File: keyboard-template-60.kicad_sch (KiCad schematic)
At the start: 168 parts, among them J1 USB_C_Receptacle_USB2.0, J2 Conn_01x04_MountingPin, SW1 SW_Reset, U1 ATmega32U4-M, U2 SRV05-4, Y1 16MHz

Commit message: Gerbers
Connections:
- net GND: now also U1.45 (Secure_to_PCB)
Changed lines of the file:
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@@
+    (stroke (width 0) (type default) (color 0 0 0 0))
+  )
+  (wire (pts (xy 346.71 127) (xy 353.06 127))
     (stroke (width 0) (type default) (color 0 0 0 0))
   )
@@
     (pin "43")
     (pin "44")
+    (pin "45")
     (pin "5")
     (pin "6")

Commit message: Update schematics and BOM
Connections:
- net COL1: now also U1.11 (PB3); no longer U1.38 (PF5)
- net ROW4: now also U1.38 (PF5); no longer U1.39 (PF4)
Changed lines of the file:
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@@
     )
   )
-  (global_label "ROW4" (shape input) (at 370.84 109.22 0) (fields_autoplaced)
+  (global_label "ROW4" (shape input) (at 370.84 111.76 0) (fields_autoplaced)
     (effects (font (size 1.27 1.27)) (justify left))
-    (property "Intersheet References" "${INTERSHEET_REFS}" (id 0) (at 378.5145 109.2994 0)
+    (property "Intersheet References" "${INTERSHEET_REFS}" (id 0) (at 378.5145 111.8394 0)
       (effects (font (size 1.27 1.27)) (justify left) hide)
     )
@@
     )
   )
-  (global_label "COL1" (shape input) (at 370.84 111.76 0) (fields_autoplaced)
+  (global_label "COL1" (shape input) (at 370.84 50.8 0) (fields_autoplaced)
     (effects (font (size 1.27 1.27)) (justify left))
-    (property "Intersheet References" "${INTERSHEET_REFS}" (id 0) (at 378.0912 111.8394 0)
+    (property "Intersheet References" "${INTERSHEET_REFS}" (id 0) (at 378.0912 50.8794 0)
       (effects (font (size 1.27 1.27)) (justify left) hide)
     )

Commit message: Final layout for prototype
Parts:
- Y1: footprint Crystal:Crystal_SMD_3225-4Pin_3.2x2.5mm_HandSoldering -> Crystal:Crystal_SMD_3225-4Pin_3.2x2.5mm
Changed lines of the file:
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@@
     (property "Reference" "Y1" (id 0) (at 298.45 78.74 90))
     (property "Value" "16MHz" (id 1) (at 298.45 81.28 90))
-    (property "Footprint" "Crystal:Crystal_SMD_3225-4Pin_3.2x2.5mm_HandSoldering" (id 2) (at 292.1 81.28 0)
+    (property "Footprint" "Crystal:Crystal_SMD_3225-4Pin_3.2x2.5mm" (id 2) (at 292.1 81.28 0)
       (effects (font (size 1.27 1.27)) hide)
     )
@@
     )
     (path "/40a982a0-a582-4b57-8a47-74dcce3e7b3f"
-      (reference "Y1") (unit 1) (value "16MHz") (footprint "Crystal:Crystal_SMD_3225-4Pin_3.2x2.5mm_HandSoldering")
-    )
-  )
+      (reference "Y1") (unit 1) (value "16MHz") (footprint "Crystal:Crystal_SMD_3225-4Pin_3.2x2.5mm")
+    )
+  )

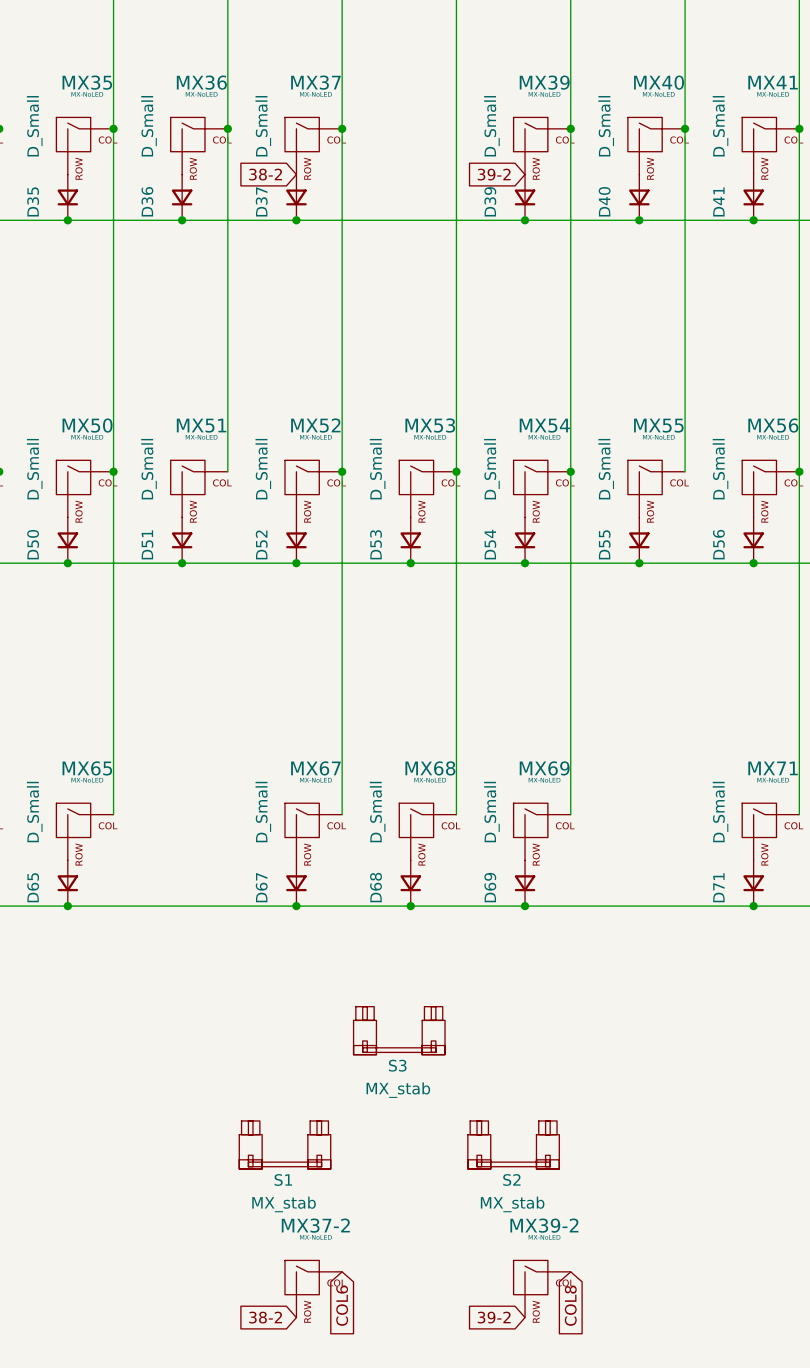
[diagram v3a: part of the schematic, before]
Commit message: Update BOM and footprint names
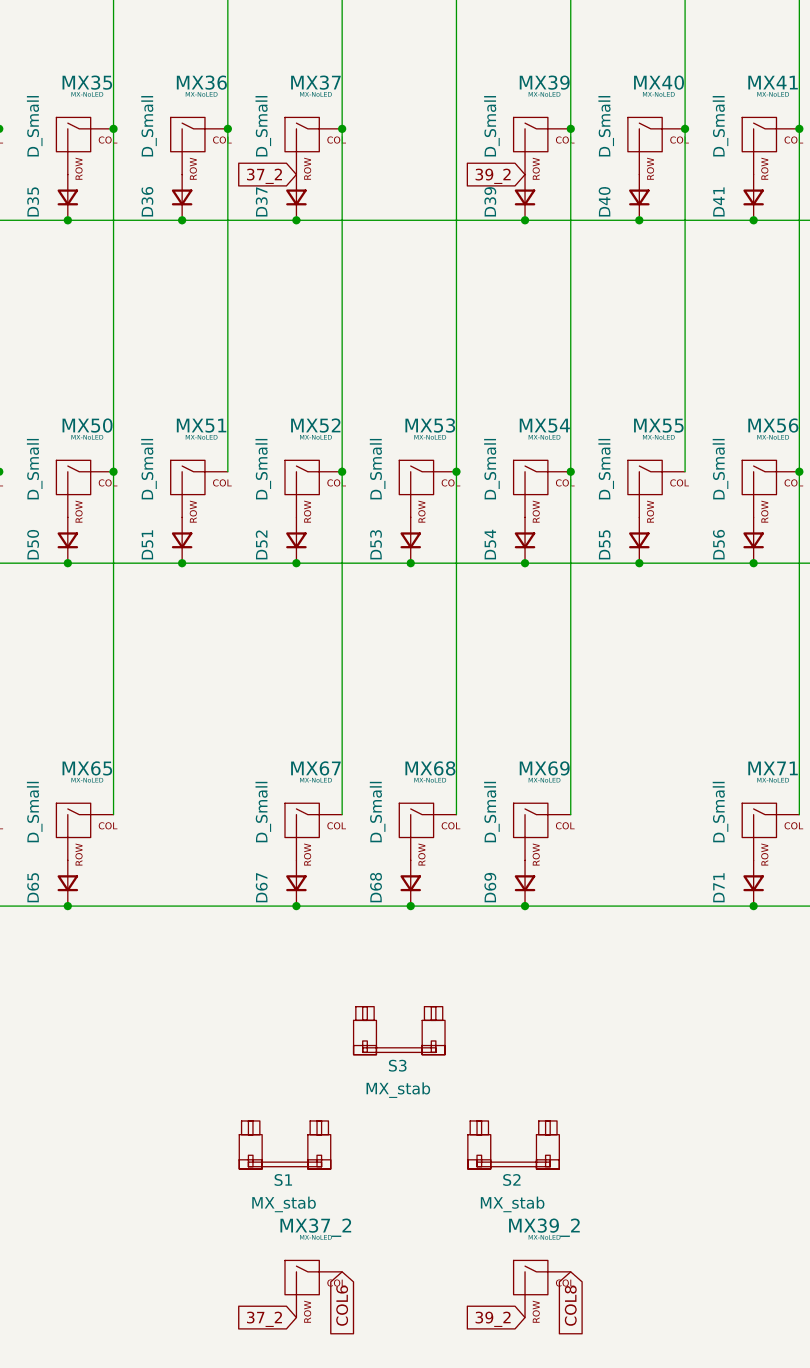
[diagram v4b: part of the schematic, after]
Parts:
- renumbered MX37-2 to MX37_2, MX39-2 to MX39_2
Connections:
- net 38-2 renamed 37_2
- net 39-2 renamed 39_2
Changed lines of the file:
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@@
     )
   )
-  (global_label "39-2" (shape input) (at 153.67 133.35 180) (fields_autoplaced)
+  (global_label "39_2" (shape input) (at 153.67 133.35 180) (fields_autoplaced)
     (effects (font (size 1.27 1.27)) (justify right))
-    (property "Intersheet References" "${INTERSHEET_REFS}" (id 0) (at 146.0559 133.2706 0)
+    (property "Intersheet References" "${INTERSHEET_REFS}" (id 0) (at 146.6607 133.2706 0)
       (effects (font (size 1.27 1.27)) (justify right) hide)
     )
@@
     )
   )
-  (global_label "38-2" (shape input) (at 128.27 260.35 180) (fields_autoplaced)
+  (global_label "37_2" (shape input) (at 128.27 260.35 180) (fields_autoplaced)
     (effects (font (size 1.27 1.27)) (justify right))
-    (property "Intersheet References" "${INTERSHEET_REFS}" (id 0) (at 120.6559 260.2706 0)
+    (property "Intersheet References" "${INTERSHEET_REFS}" (id 0) (at 121.2607 260.2706 0)
       (effects (font (size 1.27 1.27)) (justify right) hide)
     )
@@
     )
   )
-  (global_label "39-2" (shape input) (at 153.67 260.35 180) (fields_autoplaced)
+  (global_label "39_2" (shape input) (at 153.67 260.35 180) (fields_autoplaced)
     (effects (font (size 1.27 1.27)) (justify right))
-    (property "Intersheet References" "${INTERSHEET_REFS}" (id 0) (at 146.0559 260.2706 0)
+    (property "Intersheet References" "${INTERSHEET_REFS}" (id 0) (at 146.6607 260.2706 0)
       (effects (font (size 1.27 1.27)) (justify right) hide)
     )
@@
     )
   )
-  (global_label "38-2" (shape input) (at 128.27 133.35 180) (fields_autoplaced)
+  (global_label "37_2" (shape input) (at 128.27 133.35 180) (fields_autoplaced)
     (effects (font (size 1.27 1.27)) (justify right))
-    (property "Intersheet References" "${INTERSHEET_REFS}" (id 0) (at 120.6559 133.2706 0)
+    (property "Intersheet References" "${INTERSHEET_REFS}" (id 0) (at 121.2607 133.2706 0)
       (effects (font (size 1.27 1.27)) (justify right) hide)
     )
@@
   (symbol (lib_id "MX_Alps_Hybrid:MX-NoLED") (at 154.94 256.54 0) (unit 1)
     (in_bom yes) (on_board yes) (fields_autoplaced)
-    (property "Reference" "MX39-2" (id 0) (at 155.8256 250.19 0)
+    (property "Reference" "MX39_2" (id 0) (at 155.8256 250.19 0)
       (effects (font (size 1.524 1.524)))
     )
@@
   (symbol (lib_id "MX_Alps_Hybrid:MX-NoLED") (at 129.54 256.54 0) (unit 1)
     (in_bom yes) (on_board yes) (fields_autoplaced)
-    (property "Reference" "MX37-2" (id 0) (at 130.4256 250.19 0)
+    (property "Reference" "MX37_2" (id 0) (at 130.4256 250.19 0)
       (effects (font (size 1.524 1.524)))
     )
@@
     )
     (path "/f5c00a1c-6009-46f7-bb45-59e86d627cba"
-      (reference "MX37-2") (unit 1) (value "MX-NoLED") (footprint "marbastlib-mx:SW_MX_HS_1.25u")
+      (reference "MX37_2") (unit 1) (value "MX-NoLED") (footprint "marbastlib-mx:SW_MX_HS_1.25u")
     )
     (path "/75294b3a-bcf4-4dee-b1b0-009fd10bd357"
@@
     )
     (path "/a8b3e0bc-cfe9-4e81-954e-c1b4323435ec"
-      (reference "MX39-2") (unit 1) (value "MX-NoLED") (footprint "marbastlib-mx:SW_MX_HS_1.25u")
+      (reference "MX39_2") (unit 1) (value "MX-NoLED") (footprint "marbastlib-mx:SW_MX_HS_1.25u")
     )
     (path "/f1689421-be27-441f-a091-cda9d302f953"

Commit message: Updated production files
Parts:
- J2: footprint Connector_JST:JST_SH_SM04B-SRSS-TB_1x04-1MP_P1.00mm_Horizontal -> Connector_JST:JST_ACH_BM04B-ACHSS-A-GAN-ETF_1x04-1MP_P1.20mm_Vertical
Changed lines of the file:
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@@
       (effects (font (size 1.27 1.27)) (justify left))
     )
-    (property "Footprint" "Connector_JST:JST_SH_SM04B-SRSS-TB_1x04-1MP_P1.00mm_Horizontal" (id 2) (at 355.6 201.93 0)
+    (property "Footprint" "Connector_JST:JST_ACH_BM04B-ACHSS-A-GAN-ETF_1x04-1MP_P1.20mm_Vertical" (id 2) (at 355.6 201.93 0)
       (effects (font (size 1.27 1.27)) hide)
     )
@@
     )
     (path "/08e6d373-2bf3-4f1e-87e0-beb65fb65c5f"
-      (reference "J2") (unit 1) (value "Conn_01x04_MountingPin") (footprint "Connector_JST:JST_SH_SM04B-SRSS-TB_1x04-1MP_P1.00mm_Horizontal")
+      (reference "J2") (unit 1) (value "Conn_01x04_MountingPin") (footprint "Connector_JST:JST_ACH_BM04B-ACHSS-A-GAN-ETF_1x04-1MP_P1.20mm_Vertical")
     )
     (path "/bb3a180f-cdbc-49d0-97a9-6846eb214c84"

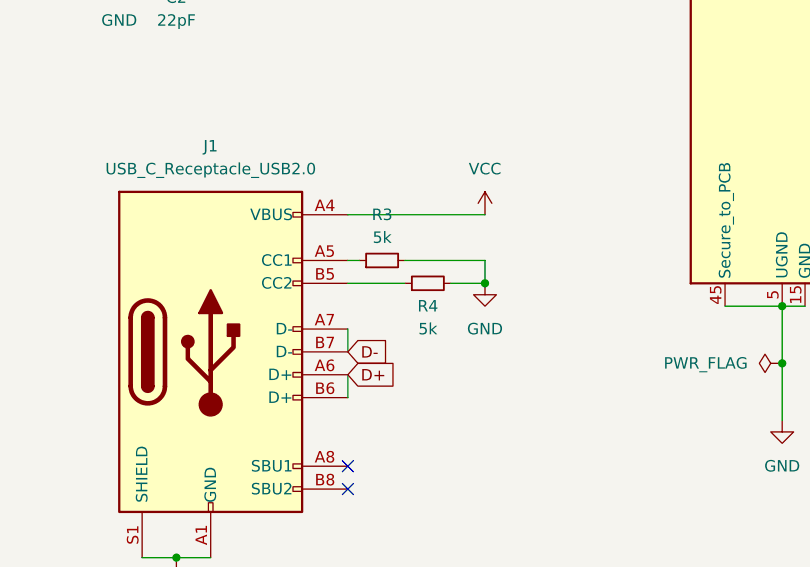
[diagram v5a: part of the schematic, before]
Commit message: Update USB-C footprint and routing
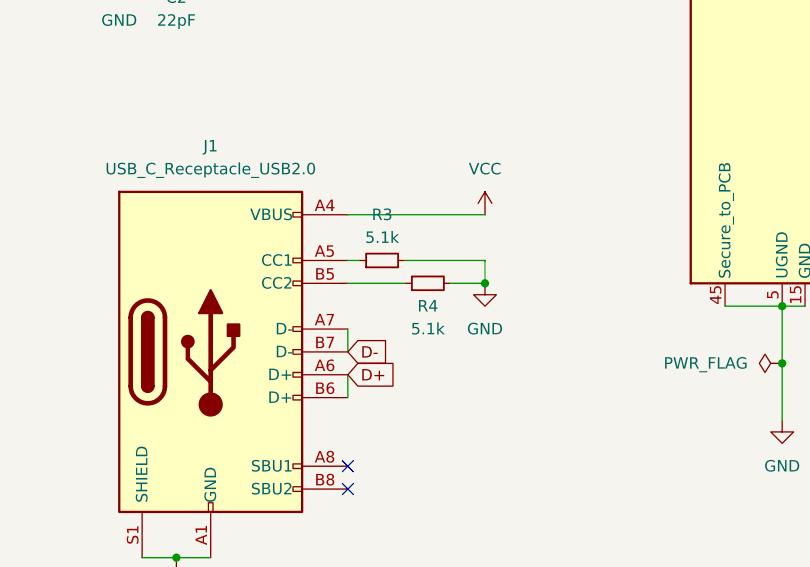
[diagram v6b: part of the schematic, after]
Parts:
- J1: footprint marbastlib-various:USB_C_Receptacle_HRO_TYPE-C-31-M-14 -> Connector_USB:USB_C_Receptacle_HRO_TYPE-C-31-M-12
- R3, R4: value 5k -> 5.1k
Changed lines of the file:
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@@
     (property "Reference" "J1" (id 0) (at 289.56 109.22 0))
     (property "Value" "USB_C_Receptacle_USB2.0" (id 1) (at 289.56 111.76 0))
-    (property "Footprint" "marbastlib-various:USB_C_Receptacle_HRO_TYPE-C-31-M-14" (id 2) (at 293.37 132.08 0)
+    (property "Footprint" "Connector_USB:USB_C_Receptacle_HRO_TYPE-C-31-M-12" (id 2) (at 293.37 132.08 0)
       (effects (font (size 1.27 1.27)) hide)
     )
@@
     (in_bom yes) (on_board yes)
     (property "Reference" "R4" (id 0) (at 313.69 127 90))
-    (property "Value" "5k" (id 1) (at 313.69 129.54 90))
+    (property "Value" "5.1k" (id 1) (at 313.69 129.54 90))
     (property "Footprint" "Capacitor_SMD:C_0603_1608Metric_Pad1.08x0.95mm_HandSolder" (id 2) (at 313.69 124.46 0)
       (effects (font (size 1.27 1.27)) hide)
@@
     (in_bom yes) (on_board yes)
     (property "Reference" "R3" (id 0) (at 308.61 116.84 90))
-    (property "Value" "5k" (id 1) (at 308.61 119.38 90))
+    (property "Value" "5.1k" (id 1) (at 308.61 119.38 90))
     (property "Footprint" "Capacitor_SMD:C_0603_1608Metric_Pad1.08x0.95mm_HandSolder" (id 2) (at 308.61 121.92 0)
       (effects (font (size 1.27 1.27)) hide)
@@
     )
     (path "/39fd6eec-df64-4ec7-90d9-dff965db8c15"
-      (reference "J1") (unit 1) (value "USB_C_Receptacle_USB2.0") (footprint "marbastlib-various:USB_C_Receptacle_HRO_TYPE-C-31-M-14")
+      (reference "J1") (unit 1) (value "USB_C_Receptacle_USB2.0") (footprint "Connector_USB:USB_C_Receptacle_HRO_TYPE-C-31-M-12")
     )
     (path "/08e6d373-2bf3-4f1e-87e0-beb65fb65c5f"
@@
     )
     (path "/65a31d27-e55c-4cca-9abe-ecfeb4877455"
-      (reference "R3") (unit 1) (value "5k") (footprint "Capacitor_SMD:C_0603_1608Metric_Pad1.08x0.95mm_HandSolder")
+      (reference "R3") (unit 1) (value "5.1k") (footprint "Capacitor_SMD:C_0603_1608Metric_Pad1.08x0.95mm_HandSolder")
     )
     (path "/542c3b37-d462-4e93-9988-5091b5e59bf5"
-      (reference "R4") (unit 1) (value "5k") (footprint "Capacitor_SMD:C_0603_1608Metric_Pad1.08x0.95mm_HandSolder")
+      (reference "R4") (unit 1) (value "5.1k") (footprint "Capacitor_SMD:C_0603_1608Metric_Pad1.08x0.95mm_HandSolder")
     )
     (path "/276330b8-e138-464f-8b38-13c9c7f3efbd"
